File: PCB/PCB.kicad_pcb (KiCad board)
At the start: 2 copper layers, 44.4 x 30.2 mm, 21 parts, among them J1 Conn_01x07_Pin, J10 Conn_01x05_Pin, J11 USB_A_PCB_Edge_receptacle, J12 Conn_01x07_Pin, J13 Conn_01x05_Pin, J14 Conn_01x05_Pin, J15 Conn_01x05_Pin, J16 Conn_01x05_Pin, J17 Conn_01x05_Pin, J9 Conn_01x05_Pin, Q1 PN2222A, Q2 PN2222A, SW1 SW_Push, SW2 SW_Push

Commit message: Added unsaved changes
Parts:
- renumbered R2 to 220Ω, R1 to 220Ω, R4 to 6.8kΩ, R3 to 6.8kΩ
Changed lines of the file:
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@@
 		(descr "Resistor, Axial_DIN0207 series, Axial, Horizontal, pin pitch=7.62mm, 0.25W = 1/4W, length*diameter=6.3*2.5mm^2, http://cdn-reichelt.de/documents/datenblatt/B400/1_4W%23YAG.pdf")
 		(tags "Resistor Axial_DIN0207 series Axial Horizontal pin pitch 7.62mm 0.25W = 1/4W length 6.3mm diameter 2.5mm")
-		(property "Reference" "R2"
+		(property "Reference" "220Ω"
 			(at 3.56 -0.05 90)
 			(layer "F.SilkS")
@@
 		(descr "Resistor, Axial_DIN0207 series, Axial, Horizontal, pin pitch=7.62mm, 0.25W = 1/4W, length*diameter=6.3*2.5mm^2, http://cdn-reichelt.de/documents/datenblatt/B400/1_4W%23YAG.pdf")
 		(tags "Resistor Axial_DIN0207 series Axial Horizontal pin pitch 7.62mm 0.25W = 1/4W length 6.3mm diameter 2.5mm")
-		(property "Reference" "R4"
+		(property "Reference" "6.8kΩ"
 			(at 4.06 0.05 90)
 			(layer "F.SilkS")
@@
 		(descr "Resistor, Axial_DIN0207 series, Axial, Horizontal, pin pitch=7.62mm, 0.25W = 1/4W, length*diameter=6.3*2.5mm^2, http://cdn-reichelt.de/documents/datenblatt/B400/1_4W%23YAG.pdf")
 		(tags "Resistor Axial_DIN0207 series Axial Horizontal pin pitch 7.62mm 0.25W = 1/4W length 6.3mm diameter 2.5mm")
-		(property "Reference" "R1"
+		(property "Reference" "220Ω"
 			(at 3.81 -0.1 90)
 			(layer "F.SilkS")
@@
 		(descr "Resistor, Axial_DIN0207 series, Axial, Horizontal, pin pitch=7.62mm, 0.25W = 1/4W, length*diameter=6.3*2.5mm^2, http://cdn-reichelt.de/documents/datenblatt/B400/1_4W%23YAG.pdf")
 		(tags "Resistor Axial_DIN0207 series Axial Horizontal pin pitch 7.62mm 0.25W = 1/4W length 6.3mm diameter 2.5mm")
-		(property "Reference" "R3"
+		(property "Reference" "6.8kΩ"
 			(at 3.86 -0.15 90)
 			(layer "F.SilkS")

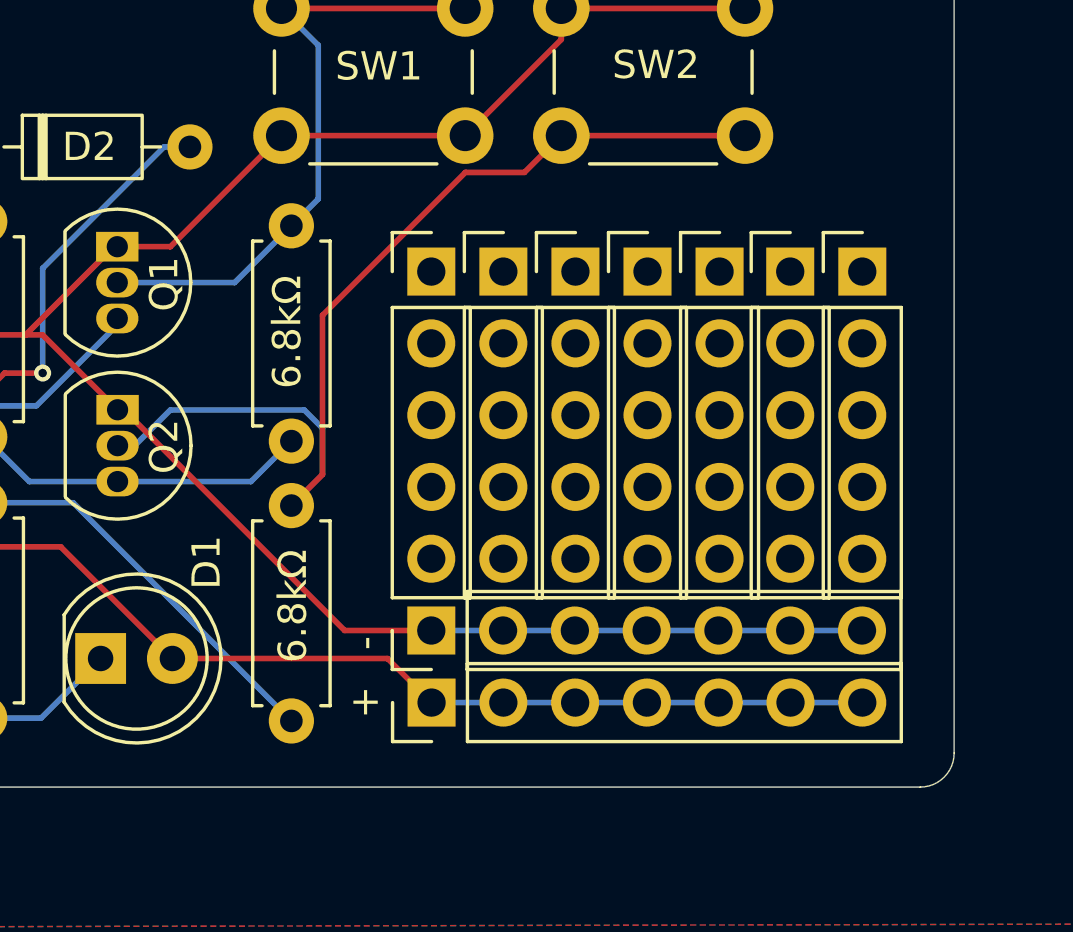
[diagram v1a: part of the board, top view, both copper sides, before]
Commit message: pcb spacing update
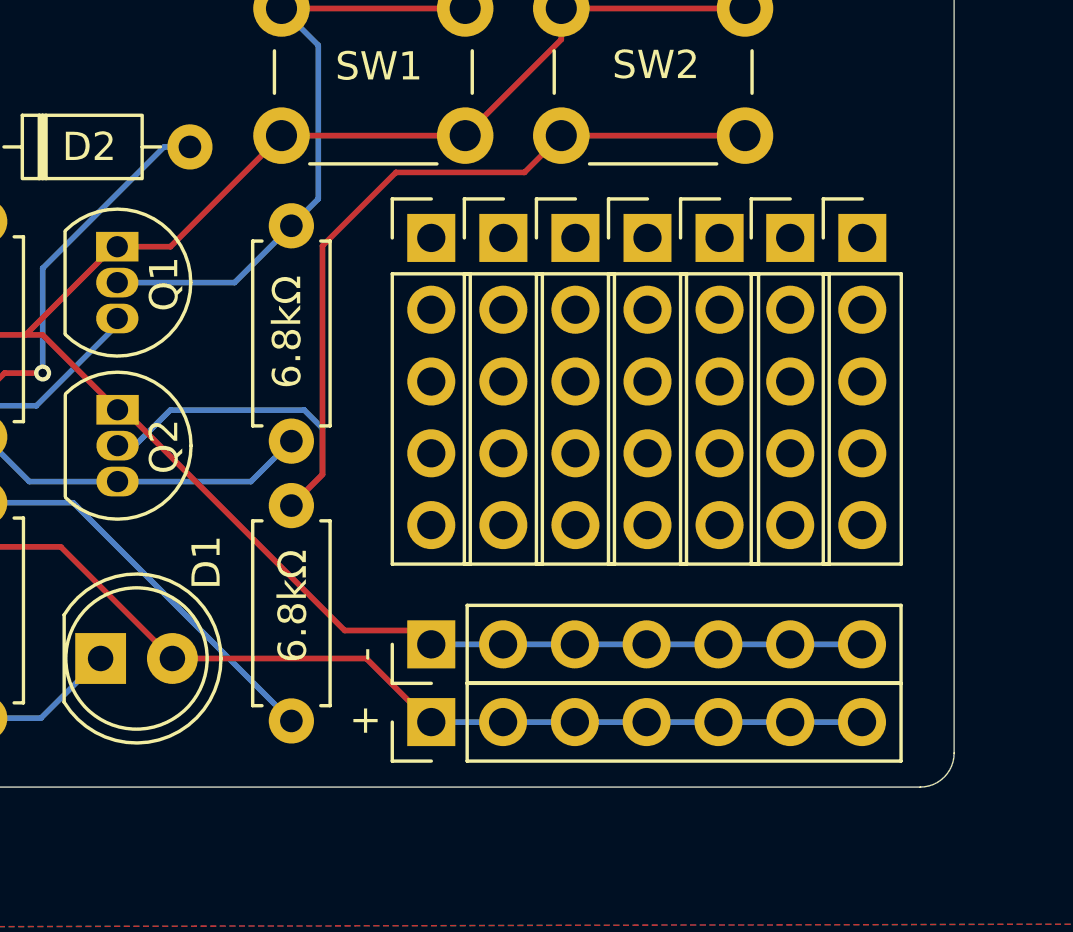
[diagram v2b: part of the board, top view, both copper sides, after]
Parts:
- moved J10 1.19 mm to (90.7, 88.7)
- moved J13 1.19 mm to (93.2, 88.7)
- moved J14 1.19 mm to (95.8, 88.7)
- moved J15 1.19 mm to (98.3, 88.7)
- moved J16 1.19 mm to (100.8, 88.7)
- moved J17 1.19 mm to (103.3, 88.7)
- moved J9 1.19 mm to (88.1, 88.7)
- moved J1 0.69 mm to (88.1, 105.8)
- moved J12 0.49 mm to (88.1, 103.0)
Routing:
- net Net-(Q2-B): track 36.0 -> 37.4 mm
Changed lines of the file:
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@@
 	(footprint "Connector_PinHeader_2.54mm:PinHeader_1x05_P2.54mm_Vertical"
 		(layer "F.Cu")
-		(at 95.75 89.86)
+		(at 95.75 88.67)
 		(descr "Through hole straight pin header, 1x05, 2.54mm pitch, single row")
 		(tags "Through hole pin header THT 1x05 2.54mm single row")
@@
 	(footprint "Connector_PinHeader_2.54mm:PinHeader_1x05_P2.54mm_Vertical"
 		(layer "F.Cu")
-		(at 100.8 89.86)
+		(at 100.8 88.67)
 		(descr "Through hole straight pin header, 1x05, 2.54mm pitch, single row")
 		(tags "Through hole pin header THT 1x05 2.54mm single row")
@@
 	(footprint "Connector_PinHeader_2.54mm:PinHeader_1x07_P2.54mm_Vertical"
 		(layer "F.Cu")
-		(at 88.11 105.11 90)
+		(at 88.1 105.8 90)
 		(descr "Through hole straight pin header, 1x07, 2.54mm pitch, single row")
 		(tags "Through hole pin header THT 1x07 2.54mm single row")
@@
 	(footprint "Connector_PinHeader_2.54mm:PinHeader_1x05_P2.54mm_Vertical"
 		(layer "F.Cu")
-		(at 98.3 89.86)
+		(at 98.3 88.67)
 		(descr "Through hole straight pin header, 1x05, 2.54mm pitch, single row")
 		(tags "Through hole pin header THT 1x05 2.54mm single row")
@@
 	(footprint "Connector_PinHeader_2.54mm:PinHeader_1x05_P2.54mm_Vertical"
 		(layer "F.Cu")
-		(at 90.65 89.86)
+		(at 90.65 88.67)
 		(descr "Through hole straight pin header, 1x05, 2.54mm pitch, single row")
 		(tags "Through hole pin header THT 1x05 2.54mm single row")
@@
 	(footprint "Connector_PinHeader_2.54mm:PinHeader_1x05_P2.54mm_Vertical"
 		(layer "F.Cu")
-		(at 103.35 89.86)
+		(at 103.35 88.67)
 		(descr "Through hole straight pin header, 1x05, 2.54mm pitch, single row")
 		(tags "Through hole pin header THT 1x05 2.54mm single row")
@@
 	(footprint "Connector_PinHeader_2.54mm:PinHeader_1x07_P2.54mm_Vertical"
 		(layer "F.Cu")
-		(at 88.1 102.56 90)
+		(at 88.1 103.05 90)
 		(descr "Through hole straight pin header, 1x07, 2.54mm pitch, single row")
 		(tags "Through hole pin header THT 1x07 2.54mm single row")
@@
 	(footprint "Connector_PinHeader_2.54mm:PinHeader_1x05_P2.54mm_Vertical"
 		(layer "F.Cu")
-		(at 88.1 89.86)
+		(at 88.1 88.67)
 		(descr "Through hole straight pin header, 1x05, 2.54mm pitch, single row")
 		(tags "Through hole pin header THT 1x05 2.54mm single row")
@@
 	(footprint "Connector_PinHeader_2.54mm:PinHeader_1x05_P2.54mm_Vertical"
 		(layer "F.Cu")
-		(at 93.2 89.86)
+		(at 93.2 88.67)
 		(descr "Through hole straight pin header, 1x05, 2.54mm pitch, single row")
 		(tags "Through hole pin header THT 1x05 2.54mm single row")
@@
 	)
 	(gr_text "+"
-		(at 85.2 105.65 0)
+		(at 85.2 106.3 0)
 		(layer "F.SilkS")
 		(effects
@@
 	)
 	(gr_text "-"
-		(at 86.35 103.25 90)
+		(at 86.35 103.65 90)
 		(layer "F.SilkS")
 		(effects
@@
 	)
 	(segment
+		(start 85.8 103.55)
+		(end 88.05 105.8)
+		(width 0.2)
+		(layer "F.Cu")
+		(net 1)
+	)
+	(segment
 		(start 73.00295 93.45)
 		(end 74.35 93.45)
@@
 	)
 	(segment
-		(start 86.55 103.55)
-		(end 88.11 105.11)
+		(start 58.15 99.6)
+		(end 53.15 99.6)
 		(width 0.2)
 		(layer "F.Cu")
@@
 	)
 	(segment
-		(start 58.15 99.6)
-		(end 53.15 99.6)
+		(start 88.05 105.8)
+		(end 88.1 105.8)
 		(width 0.2)
 		(layer "F.Cu")
@@
 	(segment
 		(start 78.94 103.55)
-		(end 86.55 103.55)
+		(end 85.8 103.55)
 		(width 0.2)
 		(layer "F.Cu")
@@
 	)
 	(segment
-		(start 93.19 105.11)
-		(end 95.73 105.11)
+		(start 93.18 105.8)
+		(end 95.72 105.8)
 		(width 0.2)
 		(layer "B.Cu")
@@
 	)
 	(segment
-		(start 90.65 105.11)
-		(end 93.19 105.11)
+		(start 90.64 105.8)
+		(end 93.18 105.8)
 		(width 0.2)
 		(layer "B.Cu")
@@
 	)
 	(segment
-		(start 100.81 105.11)
-		(end 103.35 105.11)
+		(start 100.8 105.8)
+		(end 103.34 105.8)
 		(width 0.2)
 		(layer "B.Cu")
@@
 	)
 	(segment
-		(start 88.11 105.11)
-		(end 90.65 105.11)
+		(start 88.1 105.8)
+		(end 90.64 105.8)
 		(width 0.2)
 		(layer "B.Cu")
@@
 	)
 	(segment
-		(start 95.73 105.11)
-		(end 98.27 105.11)
+		(start 95.72 105.8)
+		(end 98.26 105.8)
 		(width 0.2)
 		(layer "B.Cu")
@@
 	)
 	(segment
-		(start 98.27 105.11)
-		(end 100.81 105.11)
+		(start 98.26 105.8)
+		(end 100.8 105.8)
 		(width 0.2)
 		(layer "B.Cu")
@@
 	)
 	(segment
-		(start 85.035 102.56)
-		(end 88.1 102.56)
-		(width 0.2)
-		(layer "F.Cu")
-		(net 4)
-	)
-	(segment
 		(start 53.15 92.1)
 		(end 73.74686 92.1)
@@
 	(segment
 		(start 77 94.75)
-		(end 77.225 94.75)
+		(end 74.35 92.1)
 		(width 0.2)
 		(layer "F.Cu")
@@
 	(segment
 		(start 77 94.75)
-		(end 74.35 92.1)
+		(end 77.225 94.75)
 		(width 0.2)
 		(layer "F.Cu")
@@
 	)
 	(segment
+		(start 85.035 102.56)
+		(end 87.61 102.56)
+		(width 0.2)
+		(layer "F.Cu")
+		(net 4)
+	)
+	(segment
 		(start 77.225 94.75)
 		(end 85.035 102.56)
@@
 	)
 	(segment
+		(start 87.61 102.56)
+		(end 88.1 103.05)
+		(width 0.2)
+		(layer "F.Cu")
+		(net 4)
+	)
+	(segment
 		(start 74.35 92.1)
 		(end 73.74686 92.1)
@@
 	)
 	(segment
-		(start 93.18 102.56)
-		(end 90.64 102.56)
+		(start 93.18 103.05)
+		(end 90.64 103.05)
 		(width 0.2)
 		(layer "B.Cu")
@@
 	)
 	(segment
-		(start 98.26 102.56)
-		(end 95.72 102.56)
+		(start 98.26 103.05)
+		(end 95.72 103.05)
 		(width 0.2)
 		(layer "B.Cu")
@@
 	)
 	(segment
-		(start 100.8 102.56)
-		(end 98.26 102.56)
+		(start 100.8 103.05)
+		(end 98.26 103.05)
 		(width 0.2)
 		(layer "B.Cu")
@@
 	)
 	(segment
-		(start 95.72 102.56)
-		(end 93.18 102.56)
+		(start 95.72 103.05)
+		(end 93.18 103.05)
 		(width 0.2)
 		(layer "B.Cu")
@@
 	)
 	(segment
-		(start 90.64 102.56)
-		(end 88.1 102.56)
+		(start 90.64 103.05)
+		(end 88.1 103.05)
 		(width 0.2)
 		(layer "B.Cu")
@@
 	)
 	(segment
-		(start 103.34 102.56)
-		(end 100.8 102.56)
+		(start 103.34 103.05)
+		(end 100.8 103.05)
 		(width 0.2)
 		(layer "B.Cu")
@@
 	)
 	(segment
-		(start 89.307 86.351)
-		(end 84.251 91.407)
+		(start 92.7 85.05)
+		(end 91.399 86.351)
 		(width 0.2)
 		(layer "F.Cu")
@@
 	(segment
 		(start 91.399 86.351)
-		(end 89.307 86.351)
+		(end 86.849 86.351)
 		(width 0.2)
 		(layer "F.Cu")
@@
 	)
 	(segment
-		(start 92.7 85.05)
-		(end 91.399 86.351)
+		(start 84.251 97.039)
+		(end 83.15 98.14)
 		(width 0.2)
 		(layer "F.Cu")
@@
 	)
 	(segment
-		(start 92.7 85.05)
-		(end 99.2 85.05)
+		(start 86.849 86.351)
+		(end 84.251 88.949)
 		(width 0.2)
 		(layer "F.Cu")
@@
 	)
 	(segment
-		(start 84.251 91.407)
-		(end 84.251 97.039)
+		(start 92.7 85.05)
+		(end 99.2 85.05)
 		(width 0.2)
 		(layer "F.Cu")
@@
 	)
 	(segment
-		(start 84.251 97.039)
-		(end 83.15 98.14)
+		(start 84.251 88.949)
+		(end 84.251 97.039)
 		(width 0.2)
 		(layer "F.Cu")

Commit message: changes
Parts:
- renumbered D1 to LED, Q1 to NPN, Q2 to NPN
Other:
- board text removed: "solder.bryanhsu.app"
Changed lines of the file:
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@@
 		(descr "LED, diameter 5.0mm, 2 pins, http://cdn-reichelt.de/documents/datenblatt/A500/LL-504BC2E-009.pdf, generated by kicad-footprint-generator")
 		(tags "LED")
-		(property "Reference" "D1"
-			(at 3.75 -3.4 90)
+		(property "Reference" "LED"
+			(at 4.25 -3.3 90)
 			(layer "F.SilkS")
 			(effects
@@
 		(tags "Resistor Axial_DIN0207 series Axial Horizontal pin pitch 7.62mm 0.25W = 1/4W length 6.3mm diameter 2.5mm")
 		(property "Reference" "220Ω"
-			(at 3.56 -0.05 90)
+			(at 3.81 0 90)
 			(layer "F.SilkS")
 			(effects
@@
 		(tags "Diode DO-35_SOD27 series Axial Horizontal pin pitch 7.62mm  length 4mm diameter 2mm")
 		(property "Reference" "D2"
-			(at 4.06 0 0)
+			(at 3.11 0 0)
 			(layer "F.SilkS")
+			(hide yes)
 			(effects
 				(font
@@
 		(descr "TO-92 leads in-line, narrow, oval pads, drill 0.75mm (see NXP sot054_po.pdf)")
 		(tags "to-92 sc-43 sc-43a sot54 PA33 transistor")
-		(property "Reference" "Q1"
-			(at 1.32 -1.66 90)
+		(property "Reference" "NPN"
+			(at 1.27 -1.56 90)
 			(layer "F.SilkS")
 			(effects
@@
 		(tags "Resistor Axial_DIN0207 series Axial Horizontal pin pitch 7.62mm 0.25W = 1/4W length 6.3mm diameter 2.5mm")
 		(property "Reference" "6.8kΩ"
-			(at 4.06 0.05 90)
+			(at 3.81 0 90)
 			(layer "F.SilkS")
 			(effects
@@
 		(tags "tact sw push 6mm")
 		(property "Reference" "SW1"
-			(at 3.45 2.05 0)
+			(at 3.25 2.25 0)
 			(layer "F.SilkS")
 			(effects
@@
 		(tags "Resistor Axial_DIN0207 series Axial Horizontal pin pitch 7.62mm 0.25W = 1/4W length 6.3mm diameter 2.5mm")
 		(property "Reference" "220Ω"
-			(at 3.81 -0.1 90)
+			(at 3.81 0 90)
 			(layer "F.SilkS")
 			(effects
@@
 		(descr "TO-92 leads in-line, narrow, oval pads, drill 0.75mm (see NXP sot054_po.pdf)")
 		(tags "to-92 sc-43 sc-43a sot54 PA33 transistor")
-		(property "Reference" "Q2"
-			(at 1.3 -1.65 90)
+		(property "Reference" "NPN"
+			(at 1.25 -1.6 90)
 			(layer "F.SilkS")
 			(effects
@@
 		(tags "Resistor Axial_DIN0207 series Axial Horizontal pin pitch 7.62mm 0.25W = 1/4W length 6.3mm diameter 2.5mm")
 		(property "Reference" "6.8kΩ"
-			(at 3.86 -0.15 90)
+			(at 3.81 0 90)
 			(layer "F.SilkS")
 			(effects
@@
 			(layer "F.Fab")
 		)
+		(fp_text user "${REFERENCE}"
+			(at 0 5.08 90)
+			(layer "F.Fab")
+			(effects
+				(font
+					(size 1 1)
+					(thickness 0.15)
+				)
+			)
+		)
 		(pad "1" thru_hole rect
 			(at 0 0)
@@
 		(tags "tact sw push 6mm")
 		(property "Reference" "SW2"
-			(at 3.35 2 0)
+			(at 3.25 2.25 0)
 			(layer "F.SilkS")
 			(effects
@@
 		)
 	)
-	(gr_text "solder.bryanhsu.app"
-		(at 71.25 90.7 90)
-		(layer "B.SilkS")
-		(effects
-			(font
-				(size 0.8 0.8)
-				(thickness 0.08)
-			)
-			(justify left bottom mirror)
-		)
-	)
